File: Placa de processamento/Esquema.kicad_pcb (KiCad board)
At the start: 2 copper layers, 150.2 x 80.2 mm, 23 parts, among them IC1 5V, IC2 5V

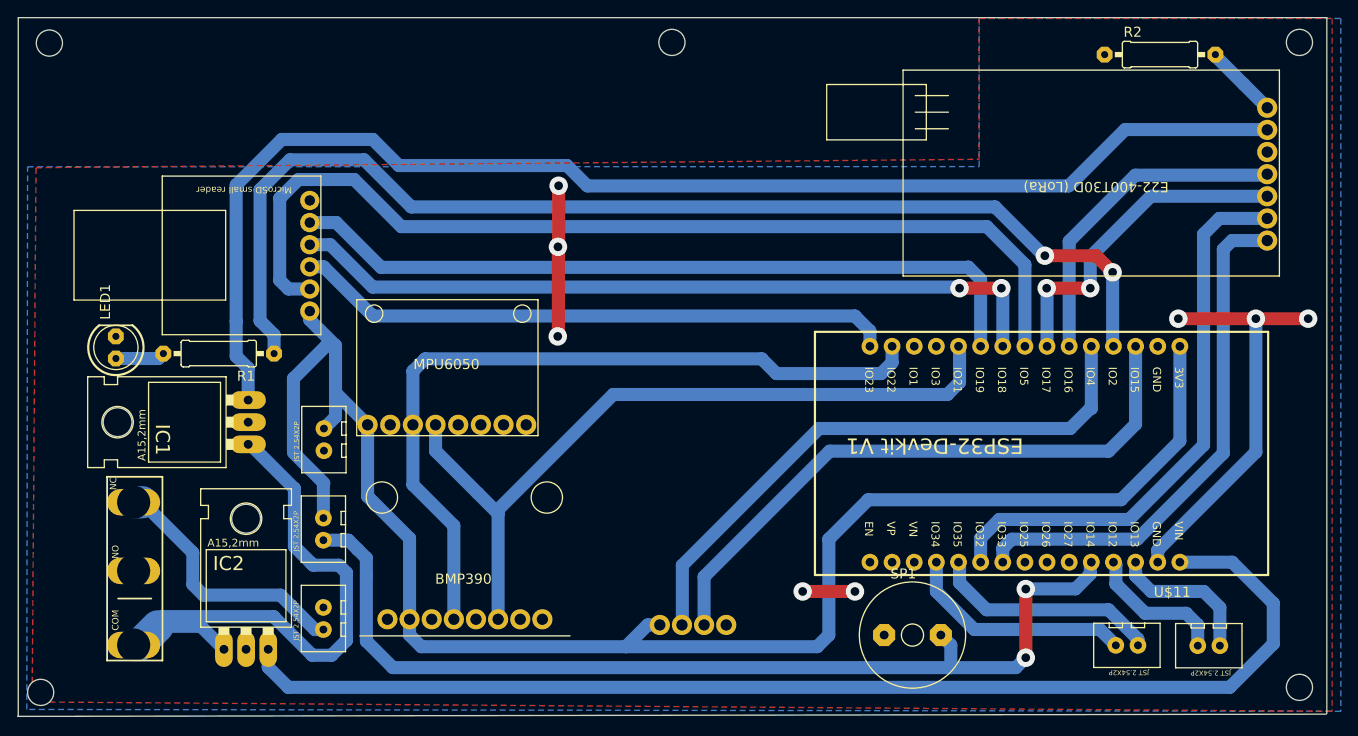
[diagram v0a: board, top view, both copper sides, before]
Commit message: Modelo 3D da placa de processamento (.f3d e .step)
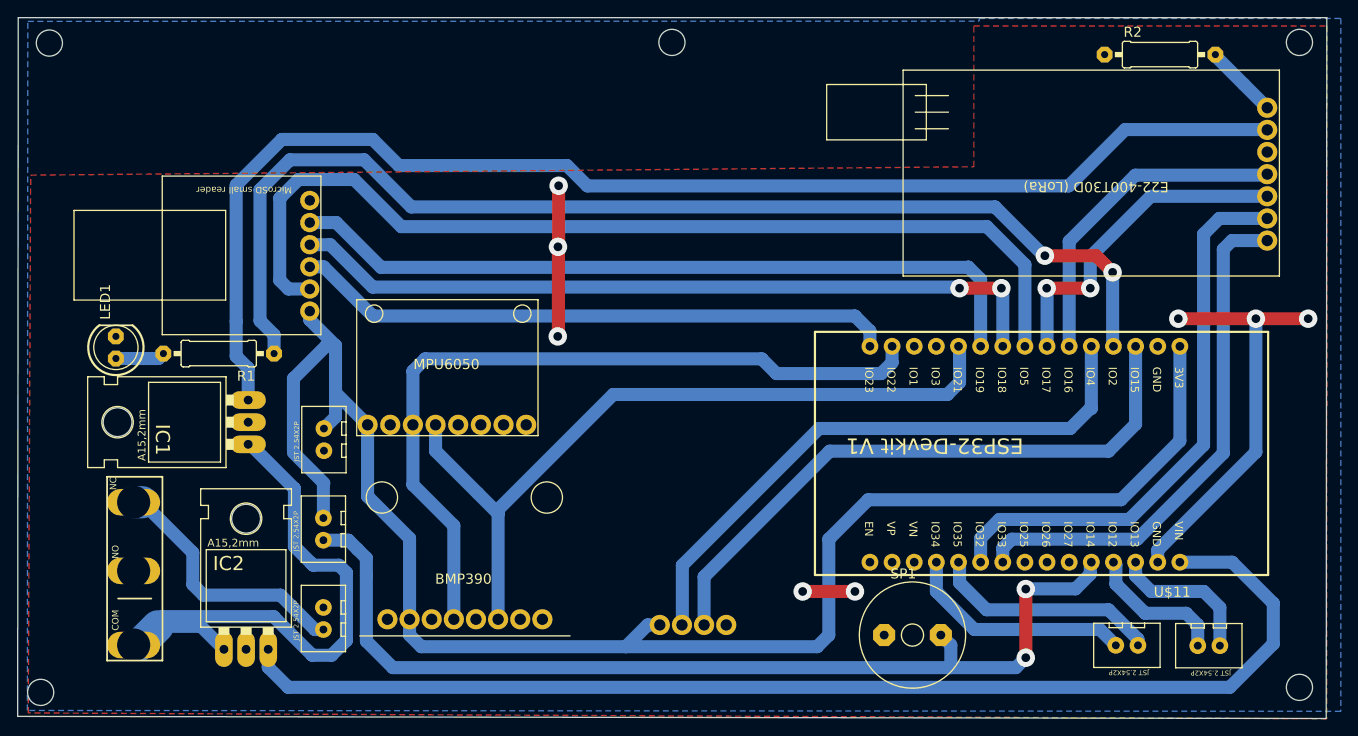
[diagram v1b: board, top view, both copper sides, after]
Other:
- board size 150.2 x 80.2 mm -> 150.2 x 80.4 mm
